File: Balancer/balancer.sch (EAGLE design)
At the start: 322 parts, among them Q1 BSS123W, Q10A SIR882DP-T1-GE3, Q10B SIS468DN-T1-GE3, Q11A SIR882DP-T1-GE3, Q11B SIS468DN-T1-GE3, Q12A SIR882DP-T1-GE3, Q12B SIS468DN-T1-GE3, Q1A8 SIR882DP-T1-GE3, Q1B8 SIS468DN-T1-GE3, Q2 BSS123W, Q3A SIR882DP-T1-GE3, Q3B SIS468DN-T1-GE3, Q4 MMBT3906LT1G, Q4A SIR882DP-T1-GE3, Q4B SIS468DN-T1-GE3, Q5 FDN5618P, Q5A SIR882DP-T1-GE3, Q5B SIS468DN-T1-GE3, Q6 CMPT3904E_TR_PBFREE, Q6A SIR882DP-T1-GE3, Q6B SIS468DN-T1-GE3, Q9A SIR882DP-T1-GE3, Q9B SIS468DN-T1-GE3, T10 750312504, T11 750312504, T12 750312504, T3 750312504, T4 750312504, T5 750312504, T6 750312504, T8 750312504, T9 750312504, U1 LTC3300ILXE-1PBF, U2 LTC3300ILXE-1PBF

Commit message: done majority of L1 wiring
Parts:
- removed C10M, C11M, C12M, C13M, C3M, C4M, C5M, C6M, C9M: 10nF, Ilya_Teach:CAP
- removed R10K, R11K, R12K, R13K, R3K, R4K, R5K, R6K, R8K, R9K: 100, rcl:R-US_R0805
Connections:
- removed net C0_F: C13M.1, C3M.1, CN2.9, R13K.2
- removed net C10_F: C10M.1, C11M.2, CN2.6, R10K.2
- removed net C11_F: C11M.1, C12M.2, CN2.7, R11K.2
- removed net C12_F: C12M.1, CN2.8, R12K.2
- removed net C3_F: C3M.2, C4M.2, CN2.1, R3K.2
- removed net C4_F: C4M.1, C5M.2, CN2.2, R4K.2
- removed net C5_F: C5M.1, C6M.1, CN2.3, R5K.2
- removed net C6_F: C6M.2, CN2.4, R6K.2
- removed net C9_F: C10M.2, C9M.1, CN2.5, R9K.2
- removed net N$98: C9M.2, R8K.2
- net C10: now also CN2.6; no longer R10K.1
- net C11: now also CN2.7; no longer R11K.1
- net C12: now also CN2.8; no longer R12K.1
- net C3: now also CN2.1; no longer R3K.1
- net C4: now also CN2.2; no longer R4K.1
- net C5: now also CN2.3; no longer R5K.1
- net C6: now also CN2.4; no longer R6K.1, R8K.1
- net C9: now also CN2.5; no longer R9K.1
- net V-: now also CN2.9; no longer C13M.2, R13K.1

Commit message: modified position of E8 and E15
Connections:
- net BAT+: no longer E15.1, E8.1
- net BOT6_TS: now also E8.1
- net C10: now also CN2.7; no longer CN2.6
- net C11: now also CN2.8; no longer CN2.7
- net C12: now also CN2.9; no longer CN2.8
- net C3: now also CN2.2; no longer CN2.1
- net C4: now also CN2.3; no longer CN2.2
- net C5: now also CN2.4; no longer CN2.3
- net C6: now also CN2.5; no longer CN2.4
- net C9: now also CN2.6; no longer CN2.5
- net TOP6_TS: now also E15.1
- net V-: now also CN2.1; no longer CN2.9
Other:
- moved on the sheet: E15, E8
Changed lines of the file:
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@@
 <attribute name="NAME" x="-123.19" y="168.91" size="1.778" layer="95" rot="R90" align="center-left"/>
 </instance>
-<instance part="E8" gate="G$1" x="58.42" y="350.52" smashed="yes">
-<attribute name="NAME" x="53.339209375" y="353.56846875" size="1.77828125" layer="95"/>
-<attribute name="VALUE" x="53.336609375" y="345.436609375" size="1.779190625" layer="96"/>
+<instance part="E8" gate="G$1" x="60.96" y="347.98" smashed="yes">
+<attribute name="NAME" x="55.879209375" y="351.02846875" size="1.77828125" layer="95"/>
+<attribute name="VALUE" x="55.876609375" y="342.896609375" size="1.779190625" layer="96"/>
 </instance>
-<instance part="E15" gate="G$1" x="-119.38" y="157.48" smashed="yes" rot="R270">
-<attribute name="NAME" x="-116.33153125" y="162.560790625" size="1.77828125" layer="95" rot="R270"/>
+<instance part="E15" gate="G$1" x="-119.38" y="154.94" smashed="yes" rot="R270">
+<attribute name="NAME" x="-116.33153125" y="160.020790625" size="1.77828125" layer="95" rot="R270"/>
 </instance>
 <instance part="CN1" gate="G$1" x="-248.92" y="83.82" smashed="yes">
@@
 </segment>
 <segment>
-<pinref part="CN2" gate="G$1" pin="4"/>
-<wire x1="-165.1" y1="27.94" x2="-172.72" y2="27.94" width="0.1524" layer="91"/>
-<label x="-167.64" y="27.94" size="1.778" layer="95"/>
+<pinref part="CN2" gate="G$1" pin="5"/>
+<wire x1="-167.64" y1="25.4" x2="-172.72" y2="25.4" width="0.1524" layer="91"/>
+<label x="-167.64" y="25.4" size="1.778" layer="95"/>
 </segment>
 </net>
@@
 </segment>
 <segment>
-<pinref part="CN2" gate="G$1" pin="2"/>
-<wire x1="-165.1" y1="33.02" x2="-172.72" y2="33.02" width="0.1524" layer="91"/>
-<label x="-167.64" y="33.02" size="1.778" layer="95"/>
+<pinref part="CN2" gate="G$1" pin="3"/>
+<wire x1="-167.64" y1="30.48" x2="-172.72" y2="30.48" width="0.1524" layer="91"/>
+<label x="-167.64" y="30.48" size="1.778" layer="95"/>
 </segment>
 </net>
@@
 </segment>
 <segment>
-<pinref part="CN2" gate="G$1" pin="9"/>
-<wire x1="-165.1" y1="15.24" x2="-172.72" y2="15.24" width="0.1524" layer="91"/>
-<label x="-167.64" y="15.24" size="1.778" layer="95"/>
+<pinref part="CN2" gate="G$1" pin="1"/>
+<wire x1="-167.64" y1="35.56" x2="-172.72" y2="35.56" width="0.1524" layer="91"/>
+<label x="-167.64" y="35.56" size="1.778" layer="95"/>
 </segment>
 </net>
@@
 </segment>
 <segment>
-<pinref part="CN2" gate="G$1" pin="3"/>
-<wire x1="-165.1" y1="30.48" x2="-172.72" y2="30.48" width="0.1524" layer="91"/>
-<label x="-167.64" y="30.48" size="1.778" layer="95"/>
+<pinref part="CN2" gate="G$1" pin="4"/>
+<wire x1="-167.64" y1="27.94" x2="-172.72" y2="27.94" width="0.1524" layer="91"/>
+<label x="-167.64" y="27.94" size="1.778" layer="95"/>
 </segment>
 </net>
@@
 </segment>
 <segment>
-<pinref part="CN2" gate="G$1" pin="1"/>
-<wire x1="-172.72" y1="35.56" x2="-165.1" y2="35.56" width="0.1524" layer="91"/>
-<label x="-167.64" y="35.56" size="1.778" layer="95"/>
+<pinref part="CN2" gate="G$1" pin="2"/>
+<wire x1="-167.64" y1="33.02" x2="-172.72" y2="33.02" width="0.1524" layer="91"/>
+<label x="-167.64" y="33.02" size="1.778" layer="95"/>
 </segment>
 </net>
@@
 <wire x1="48.26" y1="368.3" x2="48.26" y2="370.84" width="0.1524" layer="91"/>
 <wire x1="48.26" y1="370.84" x2="30.48" y2="370.84" width="0.1524" layer="91"/>
+<pinref part="E8" gate="G$1" pin="1"/>
+<wire x1="48.26" y1="368.3" x2="50.8" y2="368.3" width="0.1524" layer="91"/>
+<wire x1="50.8" y1="368.3" x2="50.8" y2="347.98" width="0.1524" layer="91"/>
+<junction x="48.26" y="368.3"/>
 </segment>
 <segment>
@@
 </segment>
 <segment>
-<pinref part="CN2" gate="G$1" pin="5"/>
-<wire x1="-165.1" y1="25.4" x2="-172.72" y2="25.4" width="0.1524" layer="91"/>
-<label x="-167.64" y="25.4" size="1.778" layer="95"/>
+<pinref part="CN2" gate="G$1" pin="6"/>
+<wire x1="-167.64" y1="22.86" x2="-172.72" y2="22.86" width="0.1524" layer="91"/>
+<label x="-167.64" y="22.86" size="1.778" layer="95"/>
 </segment>
 </net>
@@
 </segment>
 <segment>
-<pinref part="CN2" gate="G$1" pin="6"/>
-<wire x1="-165.1" y1="22.86" x2="-172.72" y2="22.86" width="0.1524" layer="91"/>
-<label x="-167.64" y="22.86" size="1.778" layer="95"/>
+<pinref part="CN2" gate="G$1" pin="7"/>
+<wire x1="-167.64" y1="20.32" x2="-172.72" y2="20.32" width="0.1524" layer="91"/>
+<label x="-167.64" y="20.32" size="1.778" layer="95"/>
 </segment>
 </net>
@@
 </segment>
 <segment>
-<pinref part="CN2" gate="G$1" pin="7"/>
-<wire x1="-165.1" y1="20.32" x2="-172.72" y2="20.32" width="0.1524" layer="91"/>
-<label x="-167.64" y="20.32" size="1.778" layer="95"/>
+<pinref part="CN2" gate="G$1" pin="8"/>
+<wire x1="-167.64" y1="17.78" x2="-172.72" y2="17.78" width="0.1524" layer="91"/>
+<label x="-167.64" y="17.78" size="1.778" layer="95"/>
 </segment>
 </net>
@@
 </segment>
 <segment>
-<pinref part="CN2" gate="G$1" pin="8"/>
-<wire x1="-165.1" y1="17.78" x2="-172.72" y2="17.78" width="0.1524" layer="91"/>
-<label x="-167.64" y="17.78" size="1.778" layer="95"/>
+<pinref part="CN2" gate="G$1" pin="9"/>
+<wire x1="-167.64" y1="15.24" x2="-172.72" y2="15.24" width="0.1524" layer="91"/>
+<label x="-167.64" y="15.24" size="1.778" layer="95"/>
 </segment>
 </net>
@@
 <junction x="-129.54" y="185.42"/>
 <pinref part="F14" gate="G$1" pin="2"/>
-<wire x1="-119.38" y1="185.42" x2="-129.54" y2="185.42" width="0.1524" layer="91"/>
+<wire x1="-119.38" y1="185.42" x2="-124.46" y2="185.42" width="0.1524" layer="91"/>
 <label x="-127" y="187.96" size="1.778" layer="95"/>
+<pinref part="E15" gate="G$1" pin="1"/>
+<wire x1="-124.46" y1="185.42" x2="-129.54" y2="185.42" width="0.1524" layer="91"/>
+<wire x1="-119.38" y1="165.1" x2="-124.46" y2="165.1" width="0.1524" layer="91"/>
+<wire x1="-124.46" y1="165.1" x2="-124.46" y2="185.42" width="0.1524" layer="91"/>
+<junction x="-124.46" y="185.42"/>
 </segment>
 <segment>
@@
 </segment>
 <segment>
-<pinref part="F14" gate="G$1" pin="1"/>
-<pinref part="E15" gate="G$1" pin="1"/>
-<wire x1="-119.38" y1="167.64" x2="-111.76" y2="167.64" width="0.1524" layer="91"/>
-<junction x="-119.38" y="167.64"/>
 <wire x1="-111.76" y1="167.64" x2="-111.76" y2="142.24" width="0.1524" layer="91"/>
 <label x="-116.84" y="142.24" size="1.778" layer="95"/>
+<pinref part="F14" gate="G$1" pin="1"/>
+<wire x1="-119.38" y1="167.64" x2="-111.76" y2="167.64" width="0.1524" layer="91"/>
 </segment>
 <segment>
 <pinref part="F13" gate="G$1" pin="1"/>
-<pinref part="E8" gate="G$1" pin="1"/>
-<wire x1="48.26" y1="350.52" x2="48.26" y2="345.44" width="0.1524" layer="91"/>
-<junction x="48.26" y="350.52"/>
-<label x="45.72" y="342.9" size="1.778" layer="95"/>
+<wire x1="48.26" y1="345.44" x2="48.26" y2="350.52" width="0.1524" layer="91"/>
+<label x="48.26" y="342.9" size="1.778" layer="95"/>
 </segment>
 </net>

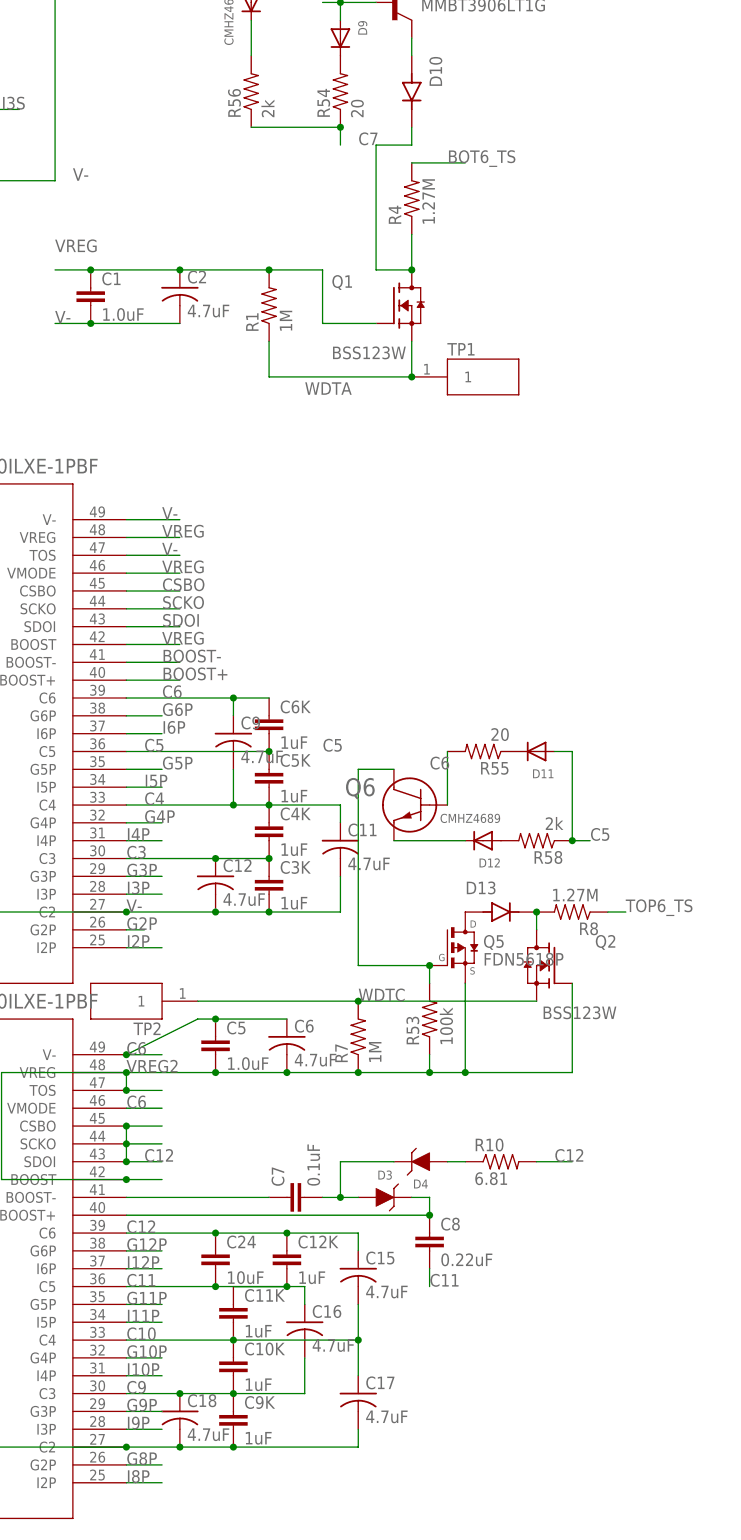
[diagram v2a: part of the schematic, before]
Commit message: finished L3 and get half of L4 done
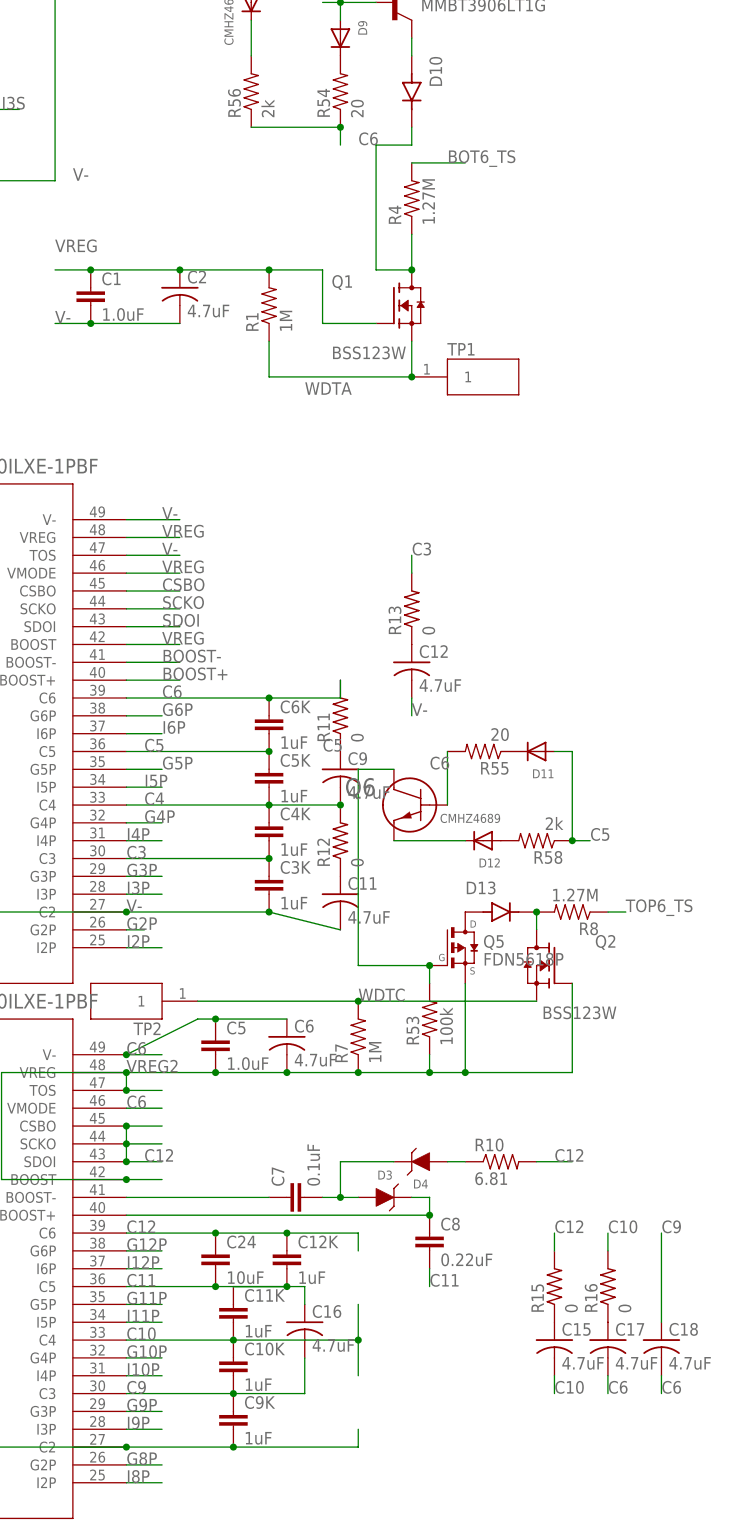
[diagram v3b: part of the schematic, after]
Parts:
- added R11, R12, R13, R15, R16: 0, rcl:R-US_R2512
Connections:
- net N$78 renamed C
- removed net C7: R54.1, R56.1
- new net N$66: C9.1, R11.1
- new net N$69: C11.1, R12.1
- new net N$71: C12.1, R13.1
- new net N$76: C15.1, R15.1
- new net N$92: C17.1, R16.1
- net C10: now also R16.2; no longer C17.1
- net C12: now also R15.2; no longer C15.1
- net C3: now also R13.2; no longer C12.1
- net C4: now also R12.2; no longer C11.1
- net C6: now also R11.2, R54.1, R56.1; no longer C9.1
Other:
- moved on the sheet: C11, C12, C15, C17, C18, C9

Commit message: Finished PCB drawing
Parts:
- removed C1A8, C1B8: 100uF, rcl:C-USC1210
- removed C1E8, C1F8, C1H8: 470pF, Ilya_Teach:CAP
- removed C1G8: 2.2nF, Ilya_Teach:CAP
- removed C1R8: 2.2uF, rcl:C-USC1210
- removed D1A8: DFLS260Q-7, balancer:DFLS260Q-7
- removed D1B8: DFLS1100-7, DFLS1100-7:DFLS1100-7
- removed D1C8: (no value), adafruit:DIODESOD-523
- removed D8E: SBR10U200P5, balancer:SBR10U200P5
- removed Q1A8: SIR882DP-T1-GE3, balancer:SIR882DP-T1-GE3
- removed Q1B8: SIS468DN-T1-GE3, SIS892DN:SIS468DN-T1-GE3
- removed R13: 0, rcl:R-US_R2512
- removed R1A8, R1B8: 20, rcl:R-US_R1206
- removed R1C8, R1F8: 5.1, Ilya_Teach:RES
- removed R1G8, R1H8: 20, Ilya_Teach:RES
- removed RS1A8: 0.005, rcl:R-US_R1206
- removed RS1B8: 0.01, rcl:R-US_R1206
- removed T8: 750312504, 750312504:750312504
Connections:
- removed net N$136: Q1A8.4, R1C8.2
- removed net N$137: D1C8.C, R1C8.1
- removed net N$138: C1A8.2, C1B8.2, C1G8.2, D1C8.A, D8E.P$1, D8E.P$2, RS1A8.1
- removed net N$139: C1E8.2, R1A8.1
- removed net N$140: C1A8.1, C1B8.1, C1E8.1, D8E.P$3, T8.1, T8.2
- removed net N$141: D1A8.1, Q1A8.5, Q1A8.6, Q1A8.7, Q1A8.8, R1A8.2, T8.10, T8.9
- removed net N$142: C1G8.1, R1G8.1
- removed net N$143: D1A8.2, Q1A8.1, Q1A8.2, Q1A8.3, R1G8.2, RS1A8.2
- removed net N$144: T8.4, T8.6
- removed net N$145: C1F8.1, R1B8.2
- removed net N$146: C1F8.2, C1R8.1, T8.7
- removed net N$147: D1B8.K, Q1B8.D, R1B8.1, T8.5
- removed net N$148: D1B8.A, Q1B8.S, R1H8.1, RS1B8.2
- removed net N$149: C1H8.2, R1H8.2
- removed net N$150: Q1B8.G, R1F8.1
- removed net N$151: R1F8.2
- removed net N$156: C1H8.1, C1R8.2, RS1B8.1
- removed net N$71: C12.1, R13.1
- net C3: now also C12.1; no longer R13.2
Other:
- moved on the sheet: F10, F4
